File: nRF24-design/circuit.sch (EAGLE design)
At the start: 9 parts, among them IC1 MEGA328-P, J1 AVR_SPI_PROG_3X2PTH, M1 WIRELESS-NRF24L01, Y1 20MHz

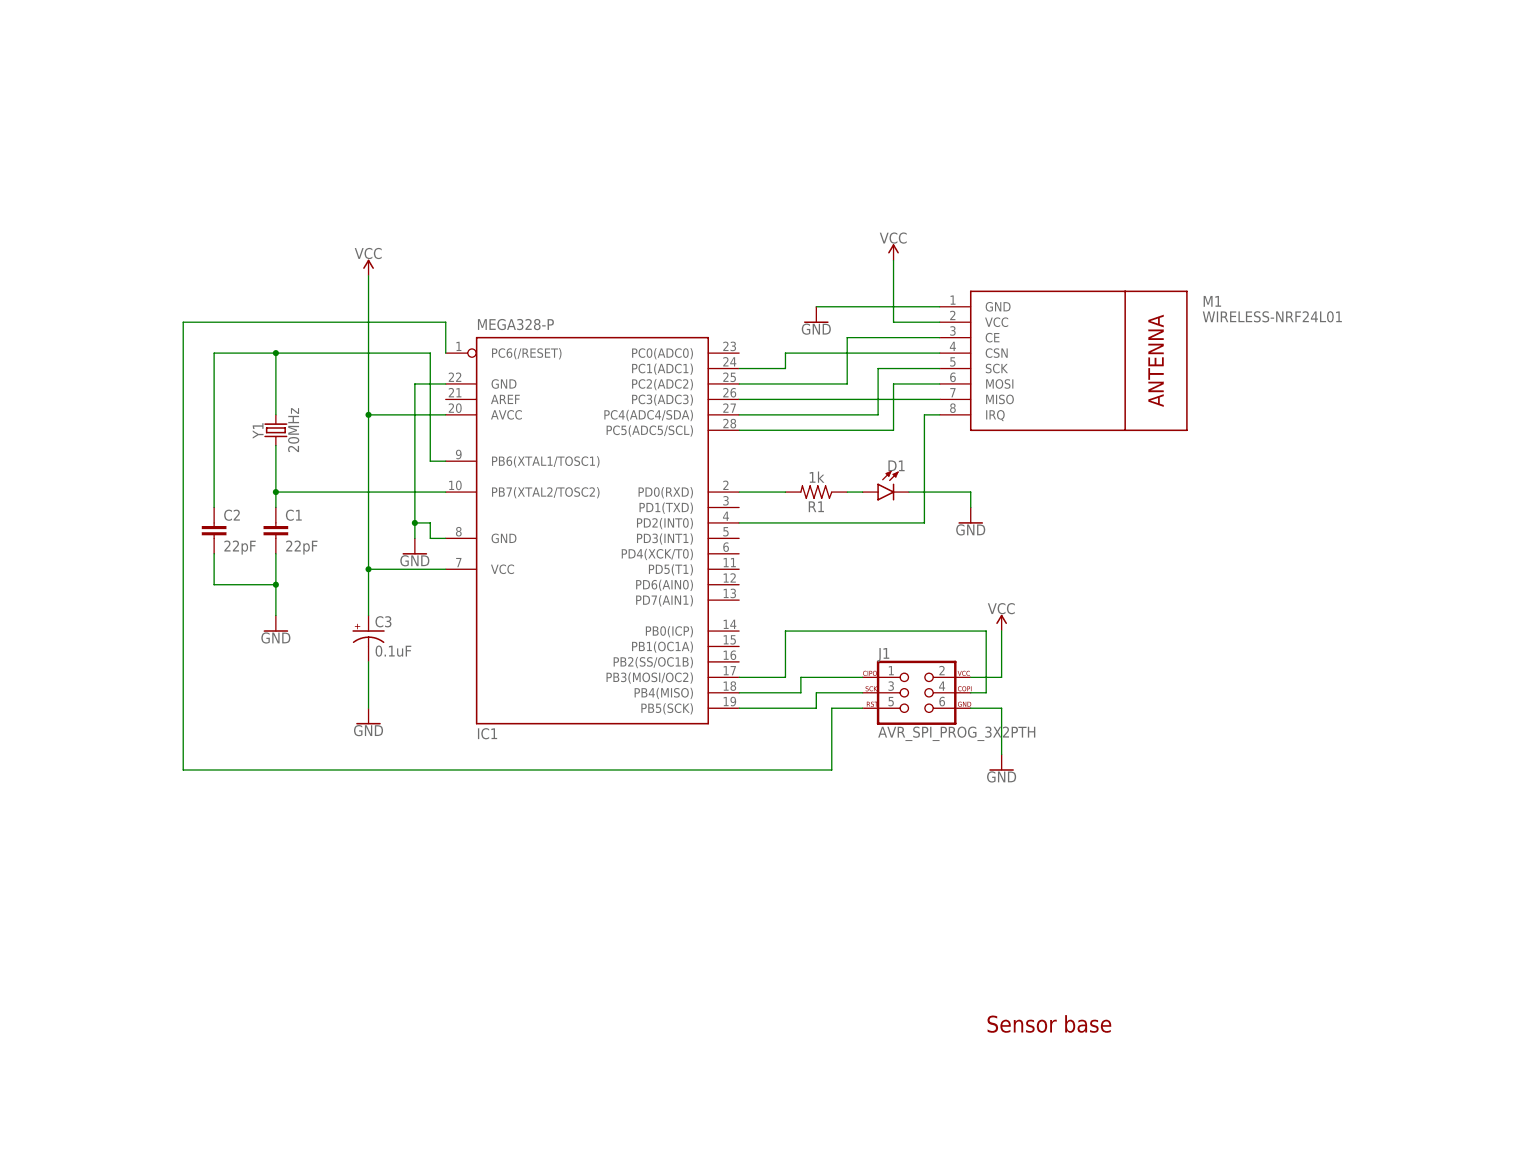
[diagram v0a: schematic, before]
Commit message: design: Fix errors (missing power and cipo connections)
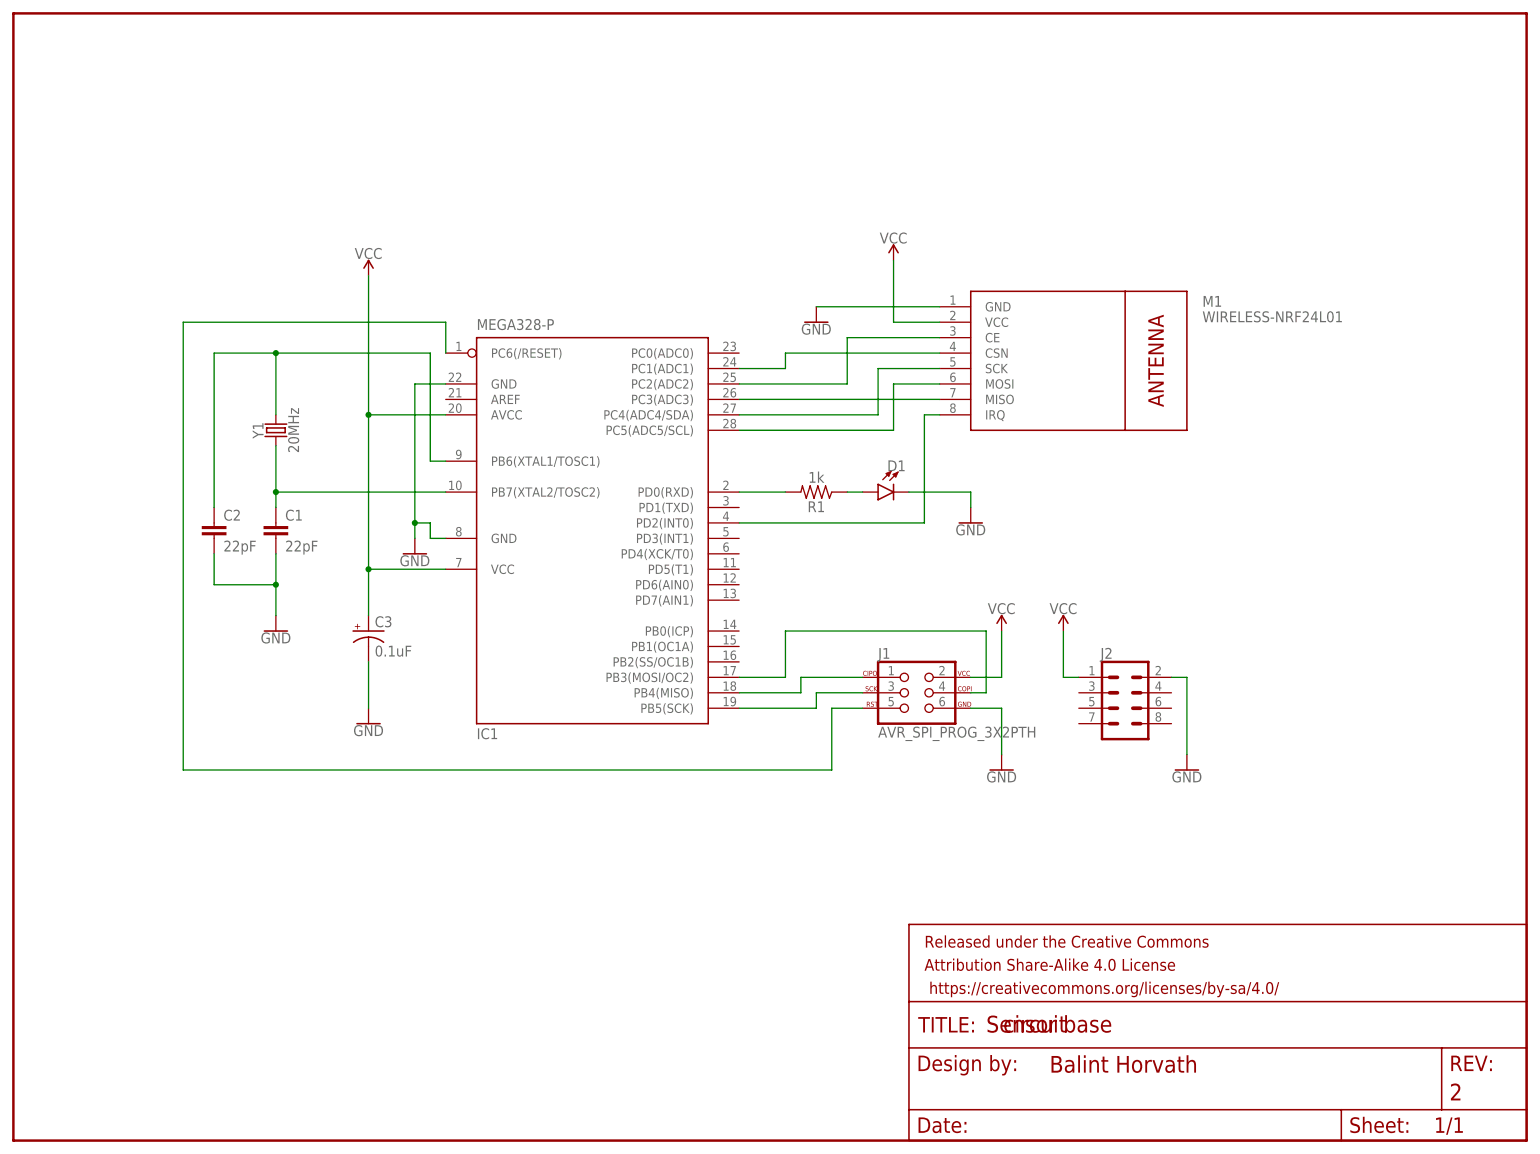
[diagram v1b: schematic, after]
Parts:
- added FRAME1: FRAME-LETTER, SparkFun-Aesthetics:FRAME-LETTER
- added J2: (no value), SparkFun-Connectors:CONN_04X2
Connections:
- net GND: now also J2.2
- net VCC: now also J2.1
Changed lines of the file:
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@@
 <part name="SUPPLY2" library="SparkFun-PowerSymbols" deviceset="VCC" device=""/>
 <part name="SUPPLY3" library="SparkFun-PowerSymbols" deviceset="VCC" device=""/>
+<part name="J2" library="SparkFun-Connectors" deviceset="CONN_04X2" device=""/>
+<part name="SUPPLY4" library="SparkFun-PowerSymbols" deviceset="VCC" device=""/>
+<part name="GND7" library="SparkFun-PowerSymbols" deviceset="GND" device=""/>
+<part name="FRAME1" library="SparkFun-Aesthetics" deviceset="FRAME-LETTER" device="">
+<attribute name="DESIGNER" value="Balint Horvath"/>
+<attribute name="REV" value="2"/>
+</part>
 </parts>
 <sheets>
@@
 <attribute name="VALUE" x="129.54" y="43.434" size="1.778" layer="96" align="bottom-center"/>
 </instance>
+<instance part="J2" gate="G$1" x="149.86" y="27.94" smashed="yes">
+<attribute name="VALUE" x="146.05" y="20.574" size="1.778" layer="96" font="vector"/>
+<attribute name="NAME" x="145.796" y="36.068" size="1.778" layer="95" font="vector"/>
+</instance>
+<instance part="SUPPLY4" gate="G$1" x="139.7" y="40.64" smashed="yes">
+<attribute name="VALUE" x="139.7" y="43.434" size="1.778" layer="96" align="bottom-center"/>
+</instance>
+<instance part="GND7" gate="1" x="160.02" y="17.78" smashed="yes">
+<attribute name="VALUE" x="160.02" y="17.526" size="1.778" layer="96" align="top-center"/>
+</instance>
+<instance part="FRAME1" gate="G$1" x="-33.02" y="-43.18" smashed="yes"/>
+<instance part="FRAME1" gate="V" x="114.3" y="-43.18" smashed="yes">
+<attribute name="LAST_DATE_TIME" x="127" y="-41.91" size="2.54" layer="94" font="vector"/>
+<attribute name="SHEET" x="200.66" y="-41.91" size="2.54" layer="94" font="vector"/>
+<attribute name="DESIGNER" x="137.414" y="-32.004" size="2.7432" layer="94" font="vector"/>
+<attribute name="REV" x="203.2" y="-36.576" size="2.7432" layer="94" font="vector"/>
+</instance>
 </instances>
 <busses>
@@
 <pinref part="GND6" gate="1" pin="GND"/>
 <wire x1="129.54" y1="27.94" x2="129.54" y2="20.32" width="0.1524" layer="91"/>
+</segment>
+<segment>
+<pinref part="J2" gate="G$1" pin="2"/>
+<wire x1="157.48" y1="33.02" x2="160.02" y2="33.02" width="0.1524" layer="91"/>
+<pinref part="GND7" gate="1" pin="GND"/>
+<wire x1="160.02" y1="33.02" x2="160.02" y2="20.32" width="0.1524" layer="91"/>
 </segment>
 </net>
@@
 <wire x1="129.54" y1="33.02" x2="124.46" y2="33.02" width="0.1524" layer="91"/>
 </segment>
-</net>
+<segment>
+<pinref part="SUPPLY4" gate="G$1" pin="VCC"/>
+<wire x1="139.7" y1="40.64" x2="139.7" y2="33.02" width="0.1524" layer="91"/>
+<pinref part="J2" gate="G$1" pin="1"/>
+<wire x1="139.7" y1="33.02" x2="142.24" y2="33.02" width="0.1524" layer="91"/>
+</segment>
+</net>

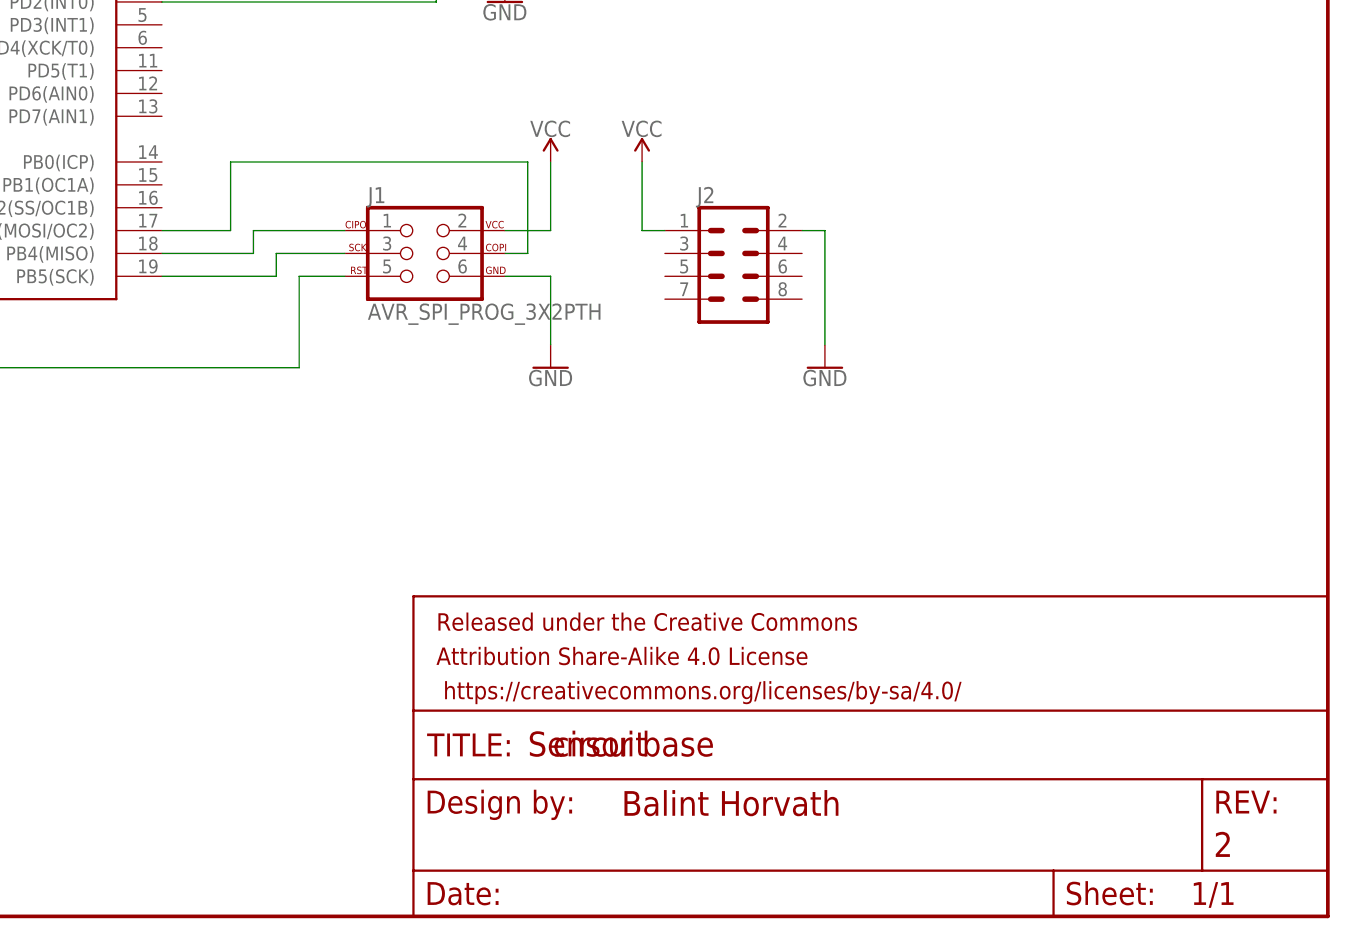
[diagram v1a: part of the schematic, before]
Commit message: design: add power connectors. Add sensor connectors
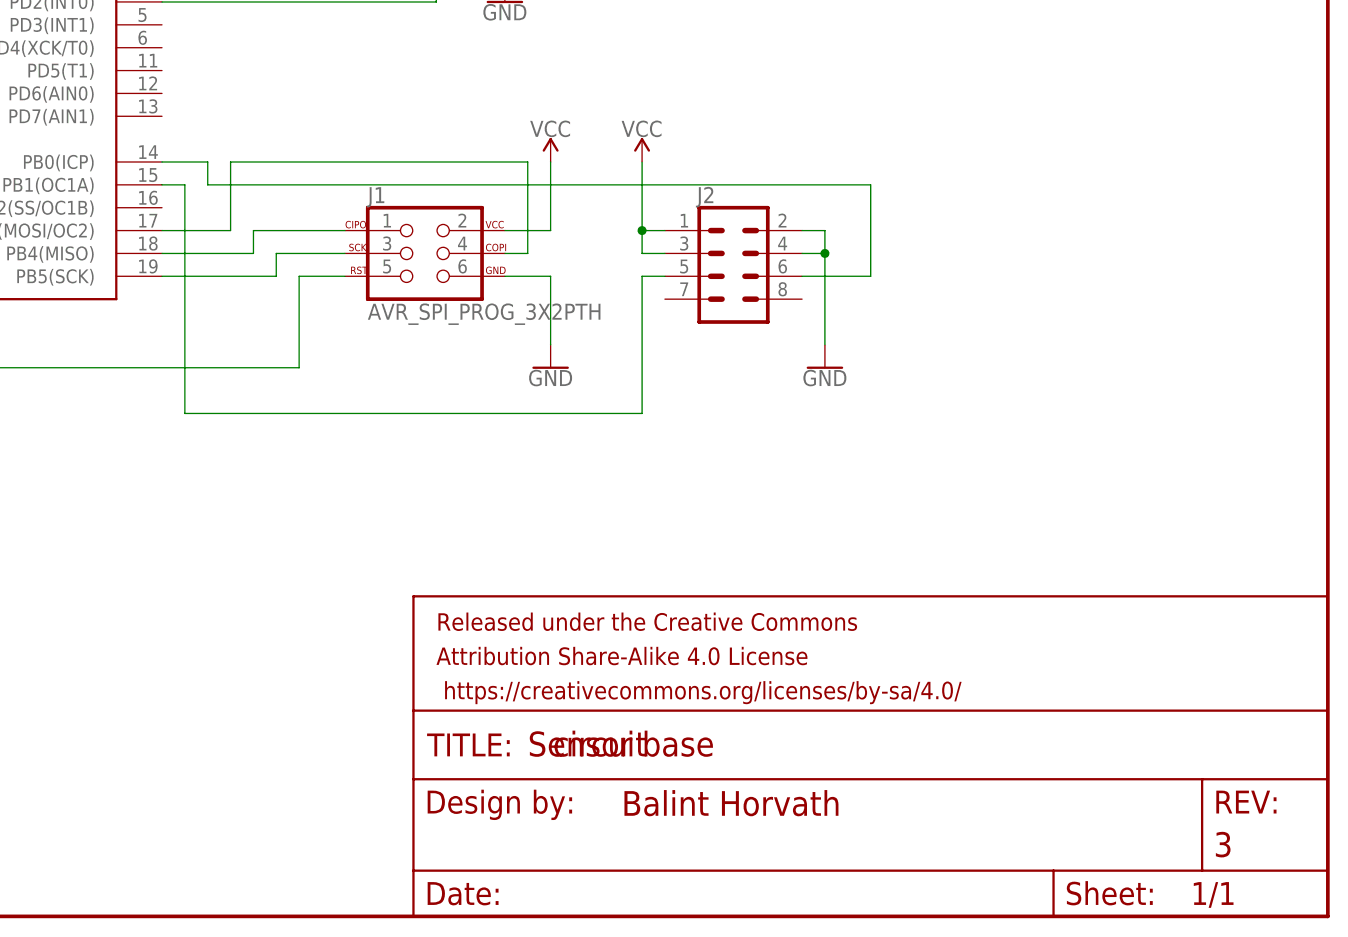
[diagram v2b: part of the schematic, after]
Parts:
- FRAME1: REV 2 -> 3
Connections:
- new net N$15: IC1.PB1(OC1A), J2.5
- new net N$17: IC1.PB0(ICP), J2.6
- net GND: now also J2.4
- net VCC: now also J2.3
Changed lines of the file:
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@@
 <part name="FRAME1" library="SparkFun-Aesthetics" deviceset="FRAME-LETTER" device="">
 <attribute name="DESIGNER" value="Balint Horvath"/>
-<attribute name="REV" value="2"/>
+<attribute name="REV" value="3"/>
 </part>
 </parts>
@@
 <wire x1="157.48" y1="33.02" x2="160.02" y2="33.02" width="0.1524" layer="91"/>
 <pinref part="GND7" gate="1" pin="GND"/>
-<wire x1="160.02" y1="33.02" x2="160.02" y2="20.32" width="0.1524" layer="91"/>
+<wire x1="160.02" y1="33.02" x2="160.02" y2="30.48" width="0.1524" layer="91"/>
+<pinref part="J2" gate="G$1" pin="4"/>
+<wire x1="160.02" y1="30.48" x2="160.02" y2="20.32" width="0.1524" layer="91"/>
+<wire x1="157.48" y1="30.48" x2="160.02" y2="30.48" width="0.1524" layer="91"/>
+<junction x="160.02" y="30.48"/>
 </segment>
 </net>
@@
 <pinref part="J2" gate="G$1" pin="1"/>
 <wire x1="139.7" y1="33.02" x2="142.24" y2="33.02" width="0.1524" layer="91"/>
+<wire x1="139.7" y1="33.02" x2="139.7" y2="30.48" width="0.1524" layer="91"/>
+<junction x="139.7" y="33.02"/>
+<pinref part="J2" gate="G$1" pin="3"/>
+<wire x1="139.7" y1="30.48" x2="142.24" y2="30.48" width="0.1524" layer="91"/>
 </segment>
 </net>
@@
 </segment>
 </net>
+<net name="N$15" class="0">
+<segment>
+<pinref part="J2" gate="G$1" pin="5"/>
+<wire x1="139.7" y1="27.94" x2="142.24" y2="27.94" width="0.1524" layer="91"/>
+<pinref part="IC1" gate="G$1" pin="PB1(OC1A)"/>
+<wire x1="86.36" y1="38.1" x2="88.9" y2="38.1" width="0.1524" layer="91"/>
+<wire x1="88.9" y1="38.1" x2="88.9" y2="12.7" width="0.1524" layer="91"/>
+<wire x1="88.9" y1="12.7" x2="139.7" y2="12.7" width="0.1524" layer="91"/>
+<wire x1="139.7" y1="12.7" x2="139.7" y2="27.94" width="0.1524" layer="91"/>
+</segment>
+</net>
+<net name="N$17" class="0">
+<segment>
+<pinref part="IC1" gate="G$1" pin="PB0(ICP)"/>
+<wire x1="86.36" y1="40.64" x2="91.44" y2="40.64" width="0.1524" layer="91"/>
+<wire x1="91.44" y1="40.64" x2="91.44" y2="38.1" width="0.1524" layer="91"/>
+<wire x1="91.44" y1="38.1" x2="165.1" y2="38.1" width="0.1524" layer="91"/>
+<wire x1="165.1" y1="38.1" x2="165.1" y2="27.94" width="0.1524" layer="91"/>
+<pinref part="J2" gate="G$1" pin="6"/>
+<wire x1="165.1" y1="27.94" x2="157.48" y2="27.94" width="0.1524" layer="91"/>
+</segment>
+</net>

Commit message: design: Align dimensions to box. Add more decoupling capacitors and labels
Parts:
- removed Y1: 20MHz, SparkFun-Clocks:CRYSTAL-16MHZPTH-HC49US
- added C4: 0.1uF, SparkFun-Capacitors:0.1UF-POLAR-RADIAL-2.5MM-25V-20%
- added Q1: 32.768KHz, crystal:CRYSTALTC26V
- added R2: 4.7k, Balint-components:1KOHM-HORIZ-1/4W-1%
- C1, C2: value 22pF -> 0.1uF; device SparkFun-Capacitors:22PF-PTH-2.54MM-200V-5% -> SparkFun-Capacitors:0.1UF-POLAR-RADIAL-2.5MM-25V-20%
- FRAME1: REV 3 -> 4
- J2: value (none) -> ZL262-8DG
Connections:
- new net N$16: J2.8, R2.1
- net GND: now also C1.-, C2.-, C4.-; no longer C1.2, C2.2
- net N$1: now also Q1.2; no longer C2.1, Y1.2
- net N$2: now also Q1.1; no longer C1.1, Y1.1
- net VCC: now also C1.+, C2.+, C4.+, R2.2
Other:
- moved on the sheet: C3
